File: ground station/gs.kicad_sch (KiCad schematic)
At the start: 23 parts, among them J1 USB_C_Receptacle_USB2.0_14P, J2 OLED, U1 ATSAMD21G18A-A, U2 SX1262IMLTRT, Y2 32MHz

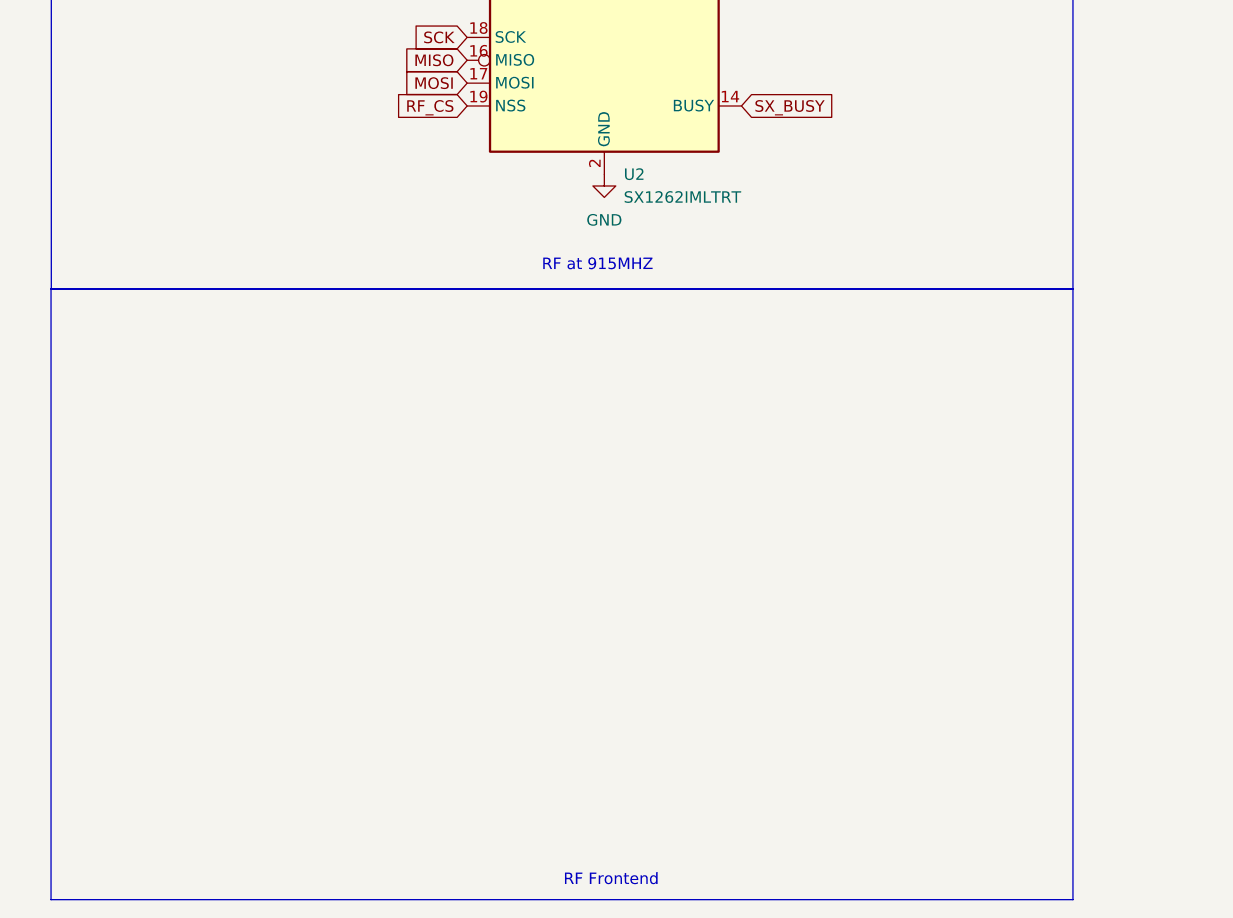
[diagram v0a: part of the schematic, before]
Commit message: more rf routing
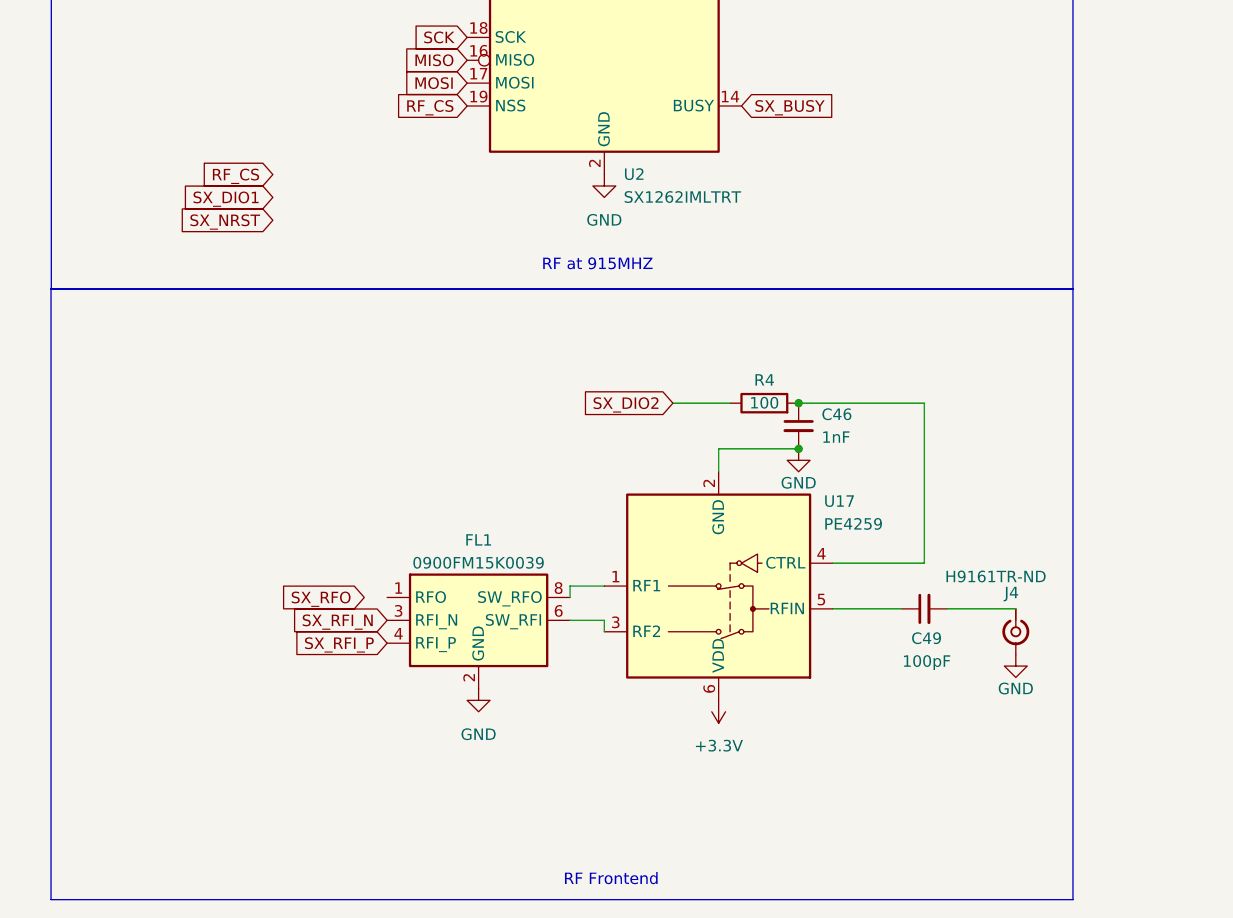
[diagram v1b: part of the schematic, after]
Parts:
- added C46: 1nF, Capacitor_SMD:C_0603_1608Metric, symbol Device:C_Small
- added C49: 100pF, Capacitor_SMD:C_0603_1608Metric, symbol Device:C_Small
- added FL1: 0900FM15K0039, RF_Converter:Balun_Johanson_0900FM15K0039, symbol Filter:0900FM15K0039
- added J4: H9161TR-ND, U.FL:HRS_U.FL-R-SMT_01_, symbol Connector:Conn_Coaxial_Small
- added R4: 100, symbol Device:R
- added U17: PE4259, Package_TO_SOT_SMD:SOT-363_SC-70-6, symbol RF_Switch_Extended:PE4259
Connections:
- net +3.3V: now also U17.6 (VDD)
- net GND: now also C46.2, FL1.10 (GND), FL1.2 (GND), FL1.5 (GND), FL1.7 (GND), FL1.9 (GND), J4.2 (Ext), U17.2 (GND)
- net SX_DIO2: now also R4.1
- net SX_RFI_N: now also FL1.3 (RFI_N)
- net SX_RFI_P: now also FL1.4 (RFI_P)
- new net: C49.1, U17.5 (RFIN)
- new net: C49.2, J4.1 (In)
- new net: FL1.6 (SW_RFI), U17.3 (RF2)
- new net: FL1.8 (SW_RFO), U17.1 (RF1)
- new net: C46.1, R4.2, U17.4 (CTRL)

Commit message: thingy for programming
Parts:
- added J7: Conn_02x03_Counter_Clockwise, Connector_PinHeader_2.54mm:PinHeader_2x03_P2.54mm_Vertical, symbol Connector_Generic:Conn_02x03_Counter_Clockwise
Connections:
- net +3.3V: now also J7.1 (Pin_1)
- net GND: now also J7.3 (Pin_3), J7.4 (Pin_4)
- net SWCLK_FLASH: now also J7.6 (Pin_6)
- net SWDIO_FLASH: now also J7.2 (Pin_2)
- net nRESET: now also J7.5 (Pin_5)
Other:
- note added: "Programming headers"

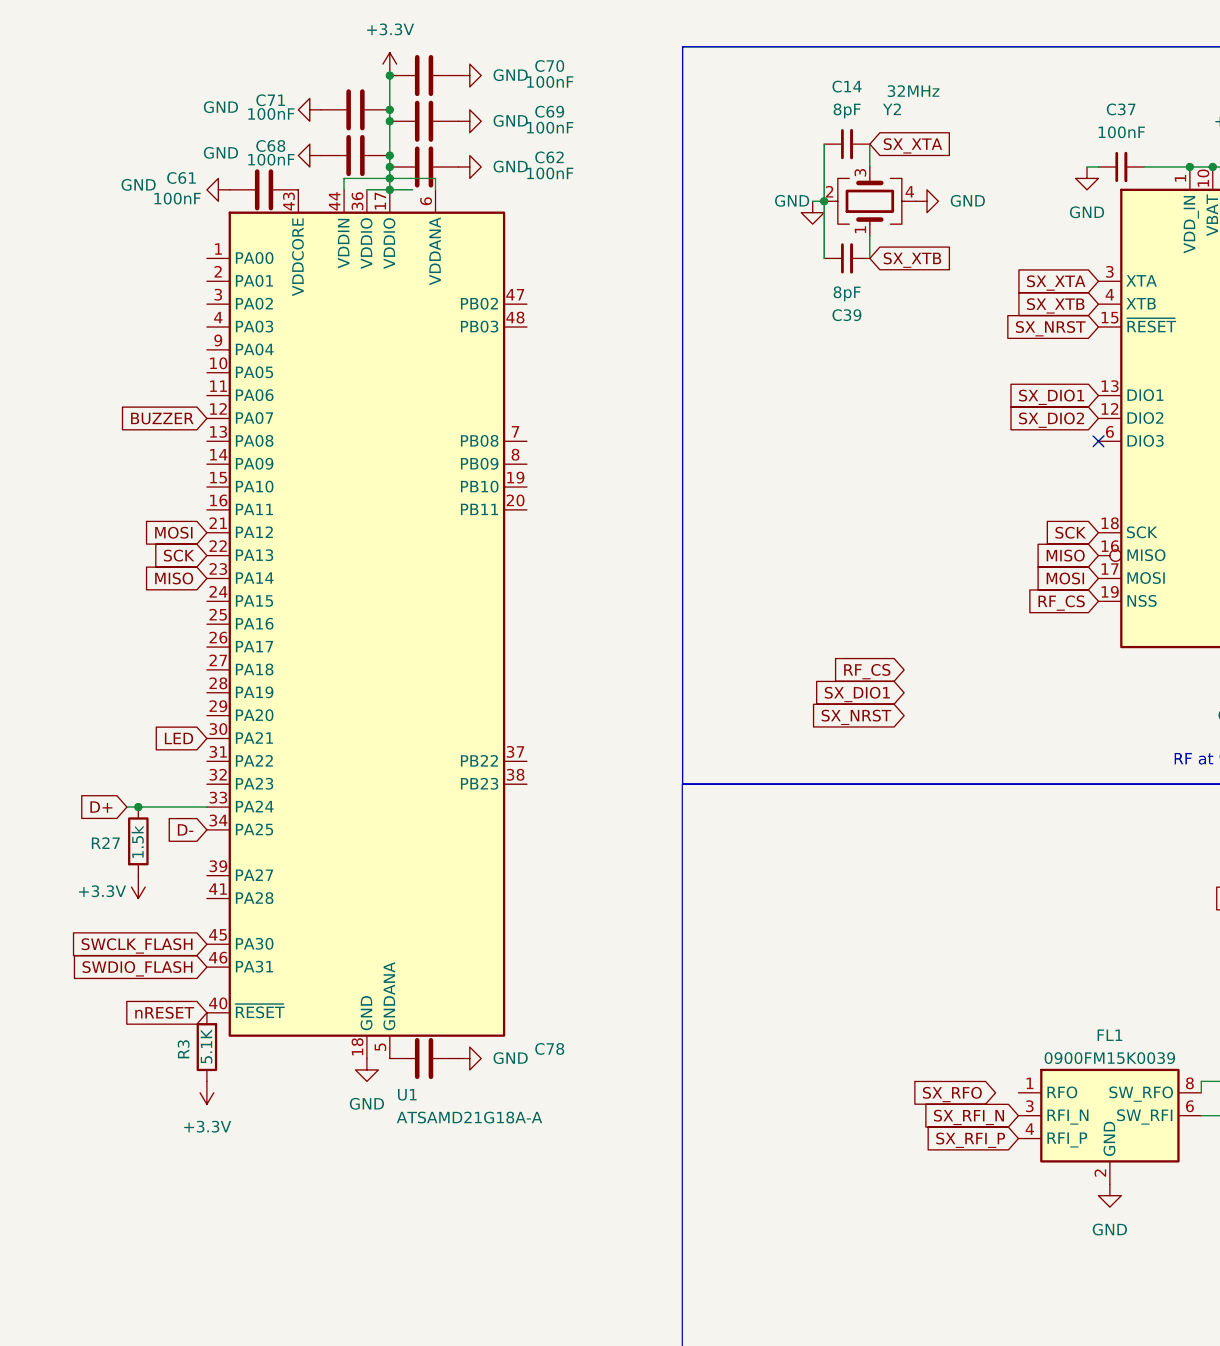
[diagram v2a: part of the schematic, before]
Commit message: schematic should be done for gs
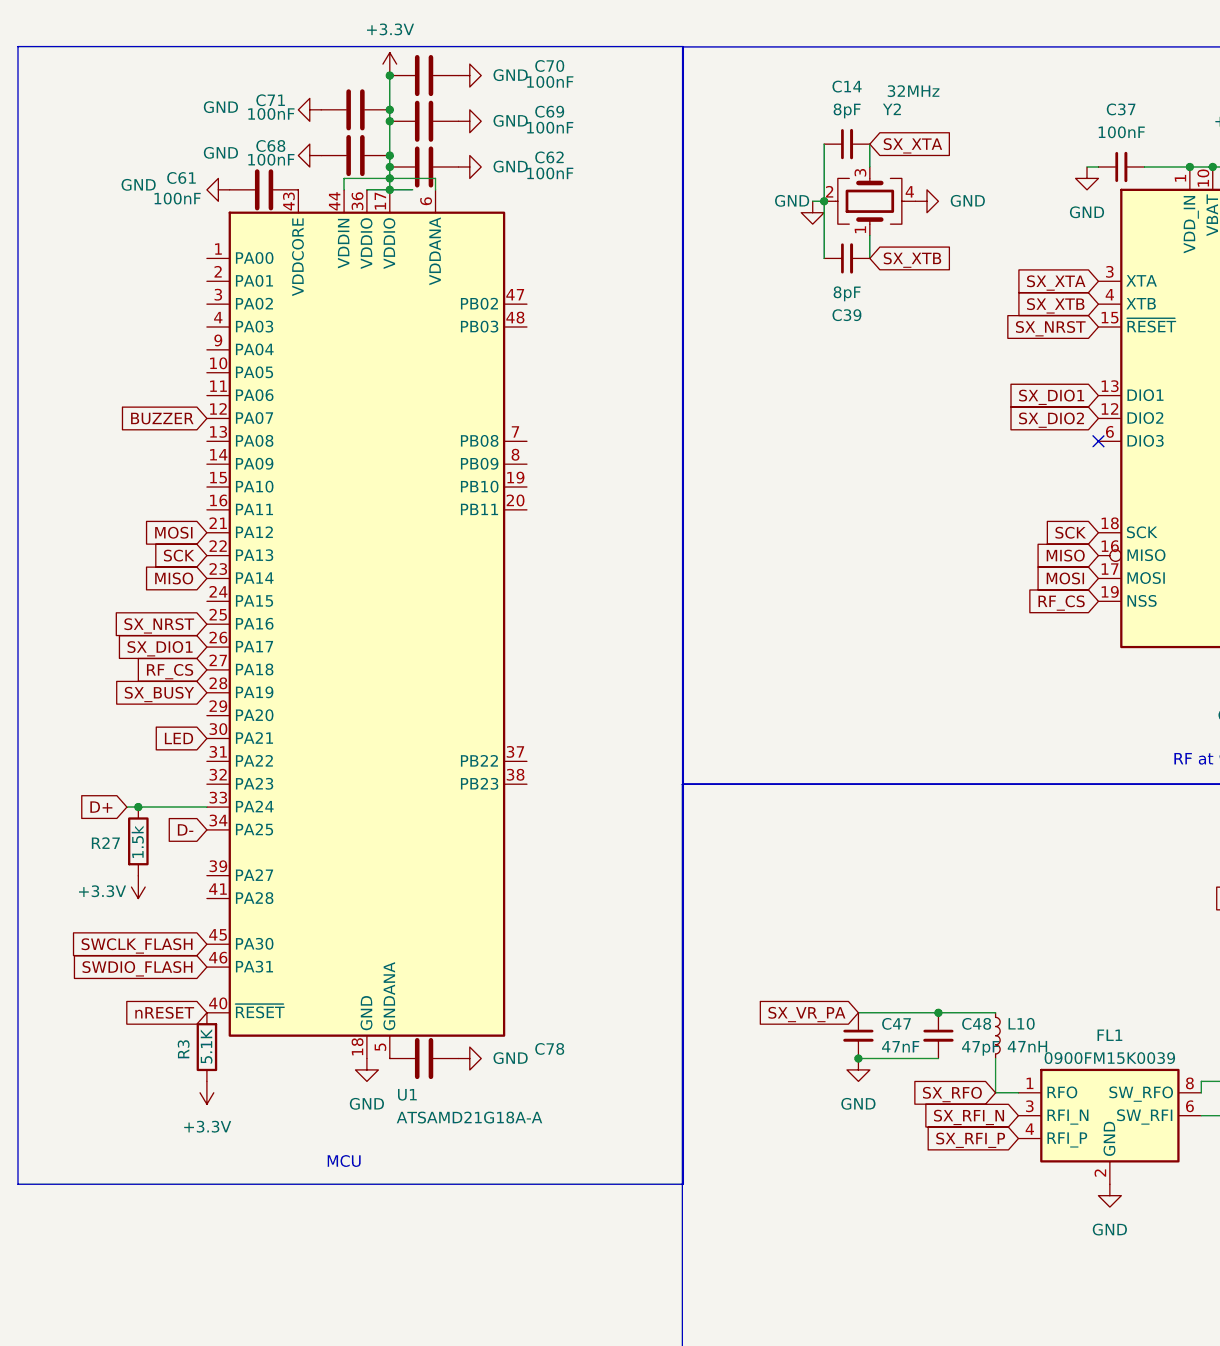
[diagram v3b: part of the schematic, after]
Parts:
- added C47: 47nF, Capacitor_SMD:C_0603_1608Metric, symbol Device:C_Small
- added C48: 47pF, Capacitor_SMD:C_0603_1608Metric, symbol Device:C_Small
- added L10: 47nH, Inductor_SMD:L_0603_1608Metric, symbol Device:L_Small
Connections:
- net GND: now also C47.2, C48.2
- net RF_CS: now also U1.27 (PA18)
- net SX_BUSY: now also U1.28 (PA19)
- net SX_DIO1: now also U1.26 (PA17)
- net SX_NRST: now also U1.25 (PA16)
- net SX_RFO: now also FL1.1 (RFO), L10.2
- net SX_VR_PA: now also C47.1, C48.1, L10.1
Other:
- note added: "MCU"

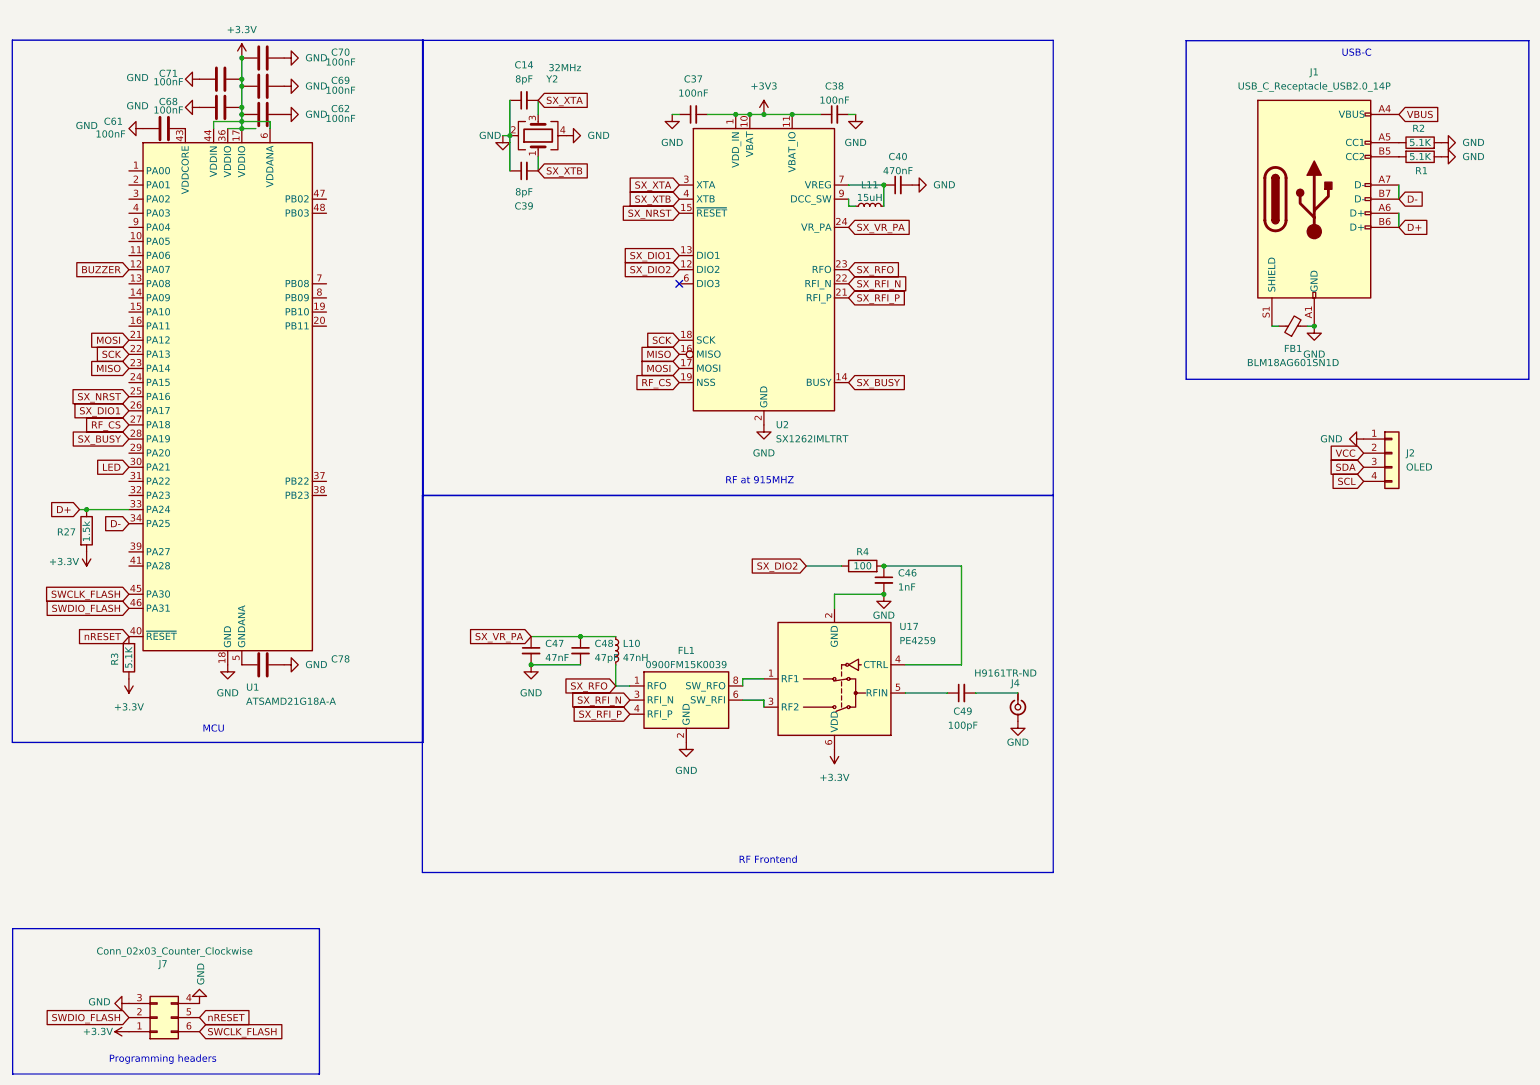
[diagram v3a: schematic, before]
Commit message: schematic fixes (3.3V and stuff) + started pcb
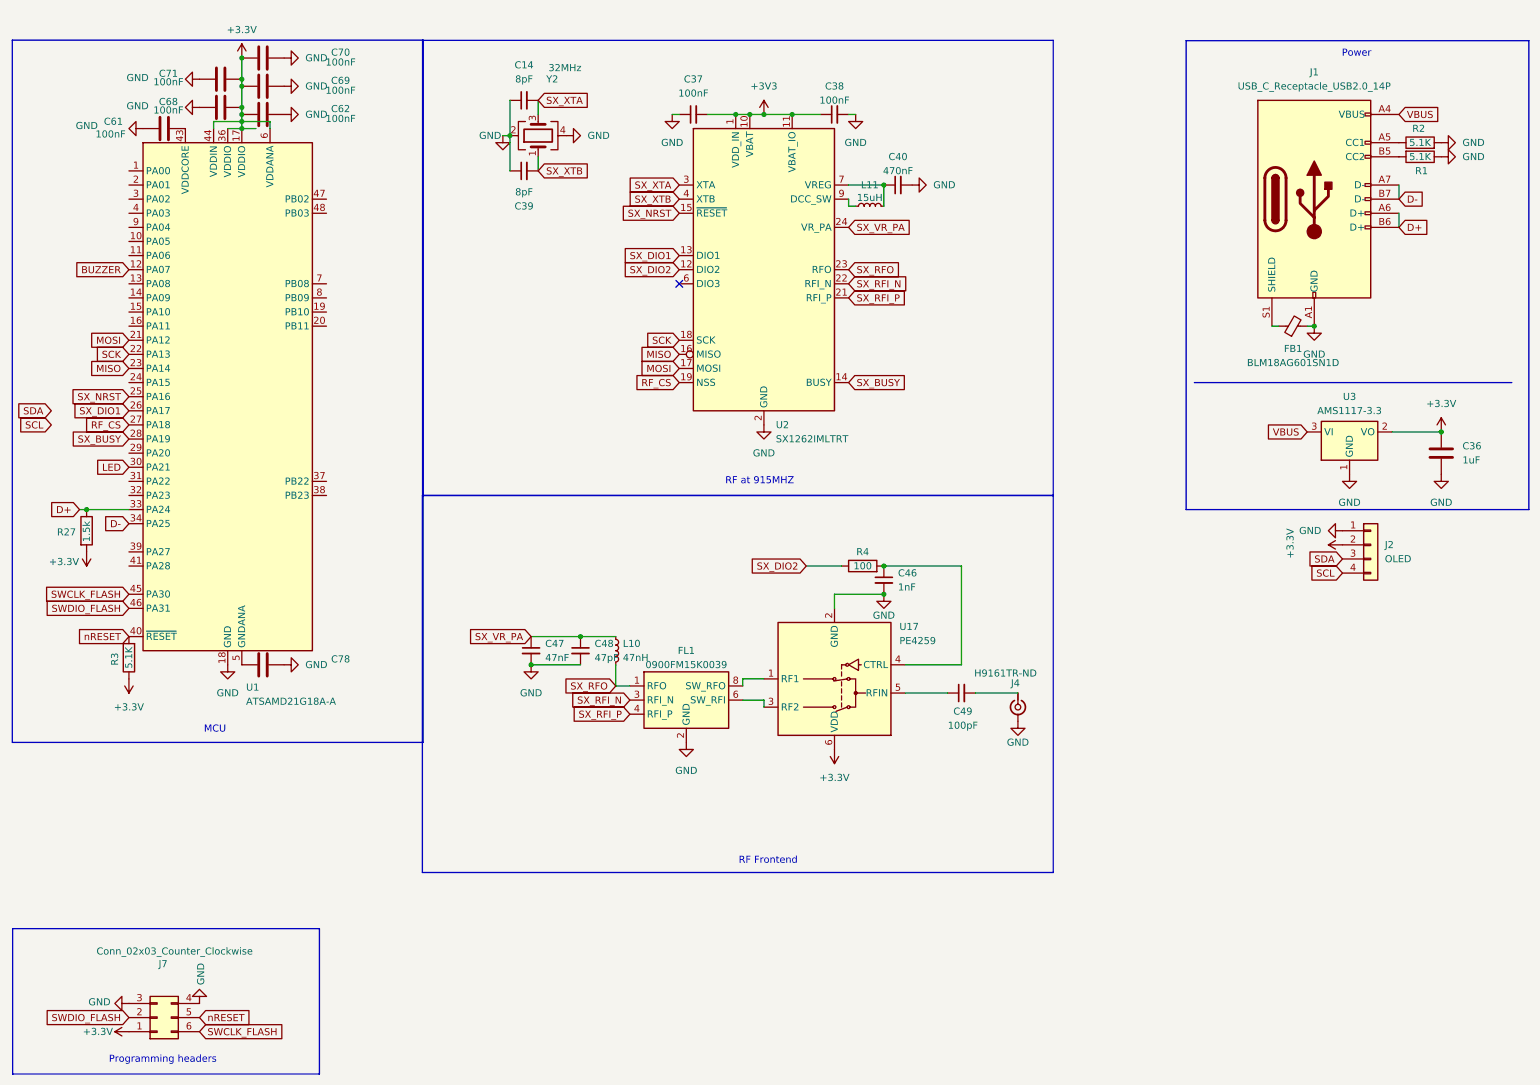
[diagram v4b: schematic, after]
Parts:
- added C36: 1uF, Capacitor_SMD:C_0603_1608Metric, symbol Device:C
- added U3: AMS1117-3.3, Package_TO_SOT_SMD:SOT-223-3_TabPin2, symbol Regulator_Linear:AMS1117-3.3
- J4: footprint U.FL:HRS_U.FL-R-SMT_01_ -> Connector_Coaxial:U.FL_Hirose_U.FL-R-SMT-1_Vertical
- R4: footprint (none) -> Resistor_SMD:R_0603_1608Metric
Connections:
- net VCC is gone; now on net +3.3V: J2.2 (Pin_2)
- net +3.3V: now also C36.1, U3.2 (VO)
- net GND: now also C36.2, U3.1 (GND)
- net VBUS: now also U3.3 (VI)
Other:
- note added: "Power"
- note removed: "USB-C"
- moved on the sheet: J2
